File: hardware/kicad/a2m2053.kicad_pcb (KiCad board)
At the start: 2 copper layers, 100 x 110 mm, 0 parts

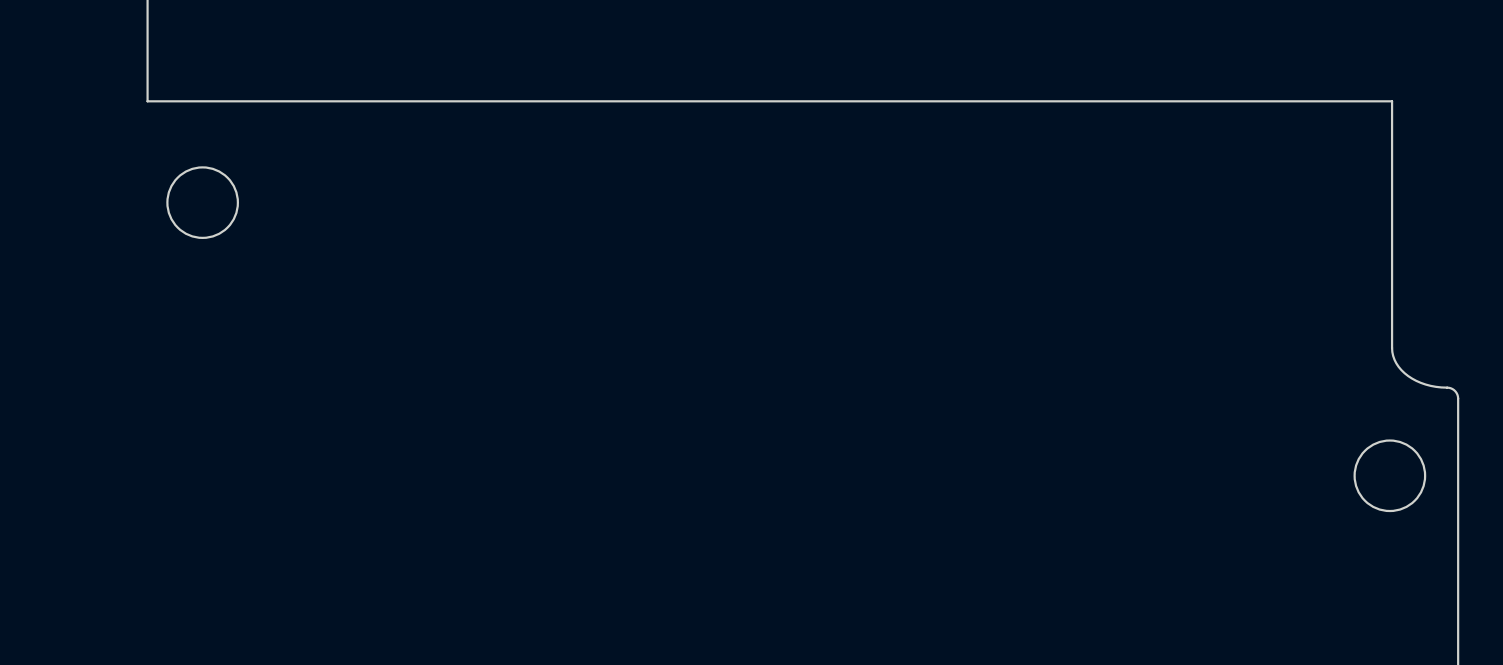
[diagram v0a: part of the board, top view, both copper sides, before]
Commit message: feat(pcb): frame-ground mounting holes H1/H2
Both M3 holes become plated footprints on net FG, placed from the
schematic. H2 uses the stock MountingHole_3.2mm_M3_Pad_Via. H1 sits
3.1 mm from the board edge, so it gets a project footprint with a
5.2 mm pad to keep 0.5 mm copper-to-edge. DRC: 0 violations; the
only unconnected item is FG between H1 and H2, not routed yet.

The outline script no longer draws hole circles; it positions H1/H2,
with a warning that footprint moves through the API crashed KiCad.

Co-Authored-By: Claude Opus 5.5 <noreply@anthropic.com>
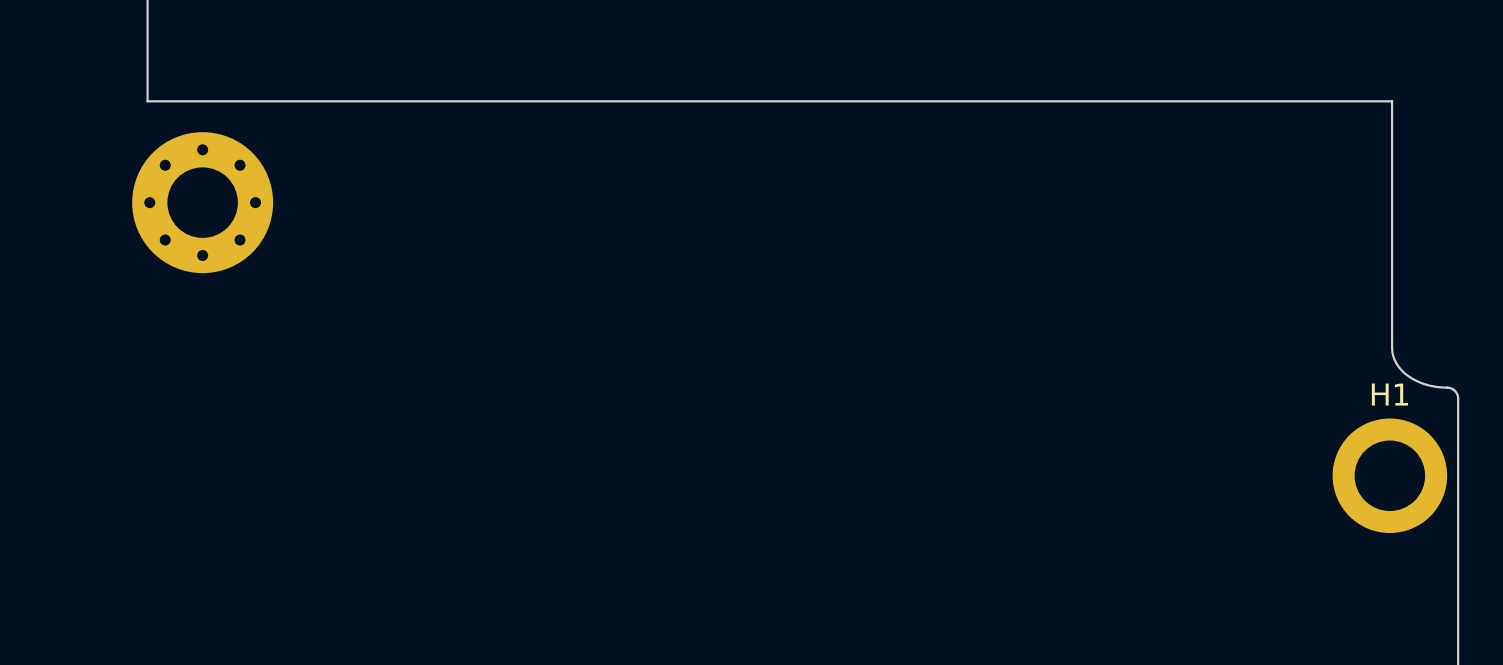
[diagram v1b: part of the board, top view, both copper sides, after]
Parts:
- added H1: M3 frame ground, a2m2053:MountingHole_3.2mm_M3_Pad_5.2mm, F.Cu at (196.9, 67.0)
- added H2: M3 frame ground, MountingHole:MountingHole_3.2mm_M3_Pad_Via, F.Cu at (143.0, 54.6)
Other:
- outline, holes or cut-outs redrawn

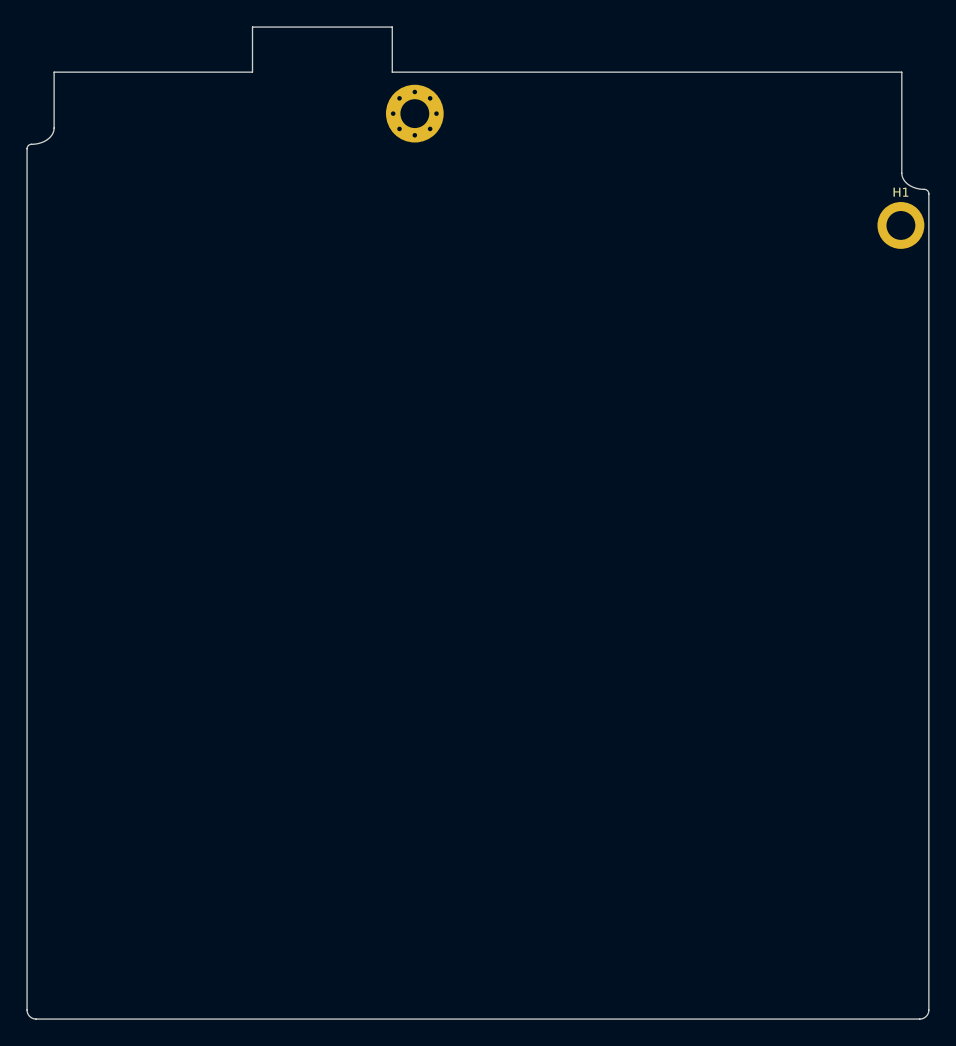
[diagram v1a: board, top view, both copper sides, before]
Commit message: feat(pcb): rear DB-19 J1 placed and fit-checked, step depths corrected
- J1: female right-angle DB-19 (daisy-chain port), 38.8 mm board-lock
  footprint on FG, face at the 94 mm top edge. Placement checked with a
  3D print holding the real connector on the IF-83 mounting points and
  in the case opening.
- Outline steps are 12 mm deep on the left and 6 mm on the right, checked
  on the IF-83. kicad_outline.py gains --outline-only.
- Photos of the fit check, EXIF stripped.

Co-Authored-By: Claude Opus 5.5 <noreply@anthropic.com>
Claude-Session: https://claude.ai/code/session_019cEGosXJSu4icn9o4uaZwB
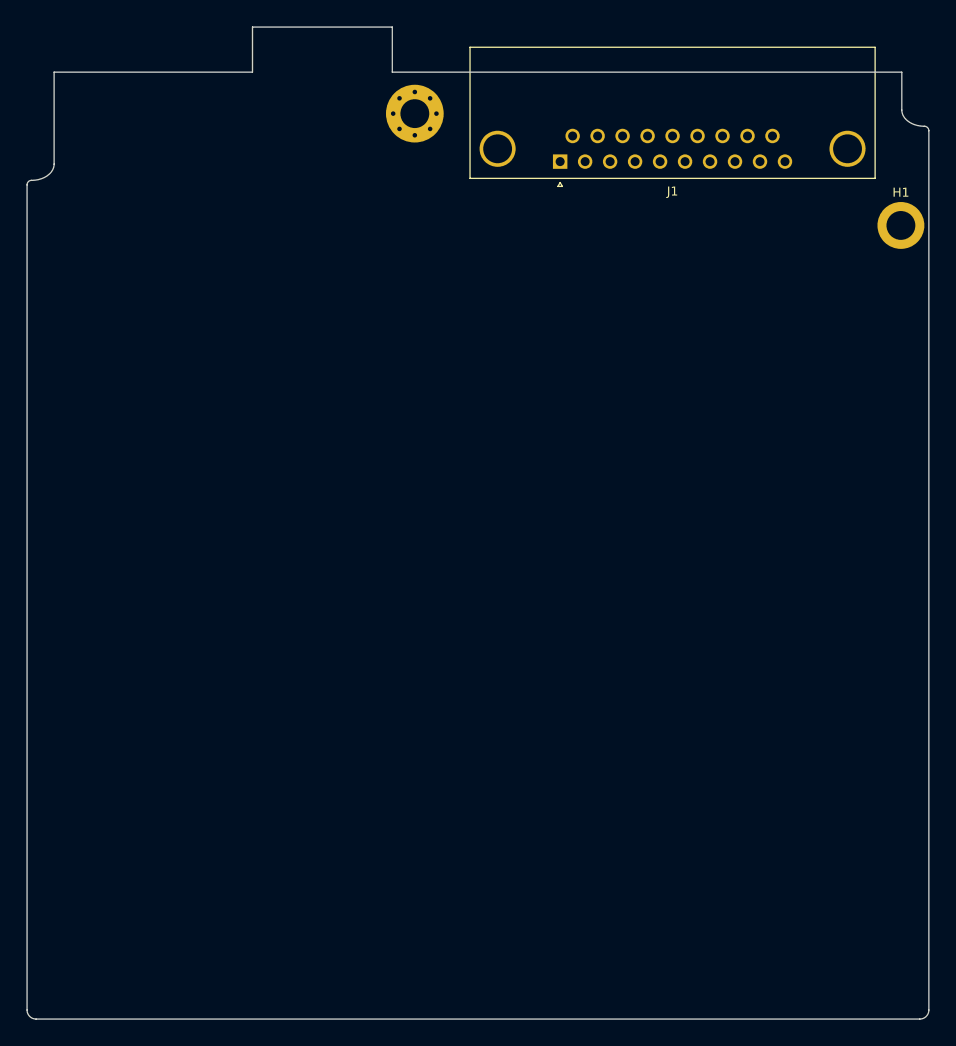
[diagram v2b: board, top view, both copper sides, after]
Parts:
- added J1: DB-19 female R/A (daisy chain), a2m2053:DSUB-19_Female_Horizontal_P2.77x2.84mm_MountingHoles38.8mm, F.Cu at (159.1, 59.9)
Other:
- outline, holes or cut-outs redrawn

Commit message: feat(pcb): schematic wired, parts placed, board autorouted
Schematic: Pico 2 (A1), five SN74LVC8T245 (U1-U5) with one 100 nF per
rail, pull-ups/pull-downs, D1 Schottky to VSYS, 4.7 uF 50 V bulk caps,
J2 (CN104) and J3 (CN102) 2x10 headers, J4 eject and J5 LED headers.

Board: all parts placed inside the IF-83 outline, Pico USB at the bottom
edge. Netclasses Power (+5V, +12V, -12V: 1.0 mm), Rail (+3V3, VSYS:
0.5 mm). GND pour on B.Cu, +5V pour on F.Cu. Tracks from Freerouting
2.1.0 (r5, 80 vias); -12V J1.5 to J3.9 routed by hand at 0.25 mm.

Routing scratch (DSN/SES runs, DRC dumps, helper scripts) lives in
hardware/kicad/scratch/, git-ignored except for its .gitkeep.

DRC: 0 unconnected. Open: EJECT via 0.42 mm from the left edge, starved
thermals on J1.4 and J3.5, silkscreen warnings, A1 library mismatch.

Co-Authored-By: Claude Opus 5.5 <noreply@anthropic.com>
Claude-Session: https://claude.ai/code/session_019cEGosXJSu4icn9o4uaZwB
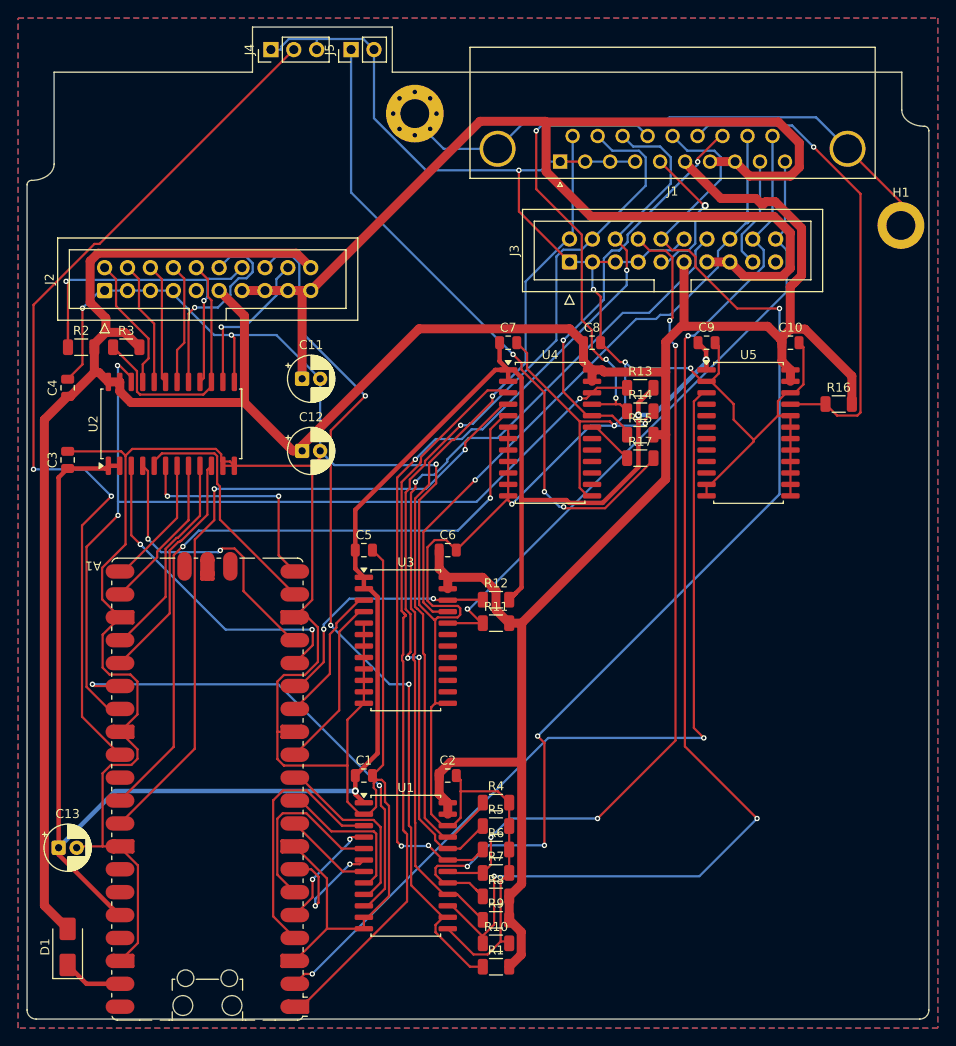
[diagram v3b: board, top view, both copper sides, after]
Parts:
- added A1: Pico 2, Module:RaspberryPi_Pico_SMD_HandSolder, F.Cu at (120.0, 129.5)
- added C1: 100nF, Capacitor_SMD:C_0805_2012Metric, F.Cu at (137.3, 128.0)
- added C10: 100nF, Capacitor_SMD:C_0805_2012Metric, F.Cu at (184.7, 80.0)
- added C11: 4.7uF 50V, Capacitor_THT:CP_Radial_D5.0mm_P2.00mm, F.Cu at (130.5, 84.0)
- added C12: 4.7uF 50V, Capacitor_THT:CP_Radial_D5.0mm_P2.00mm, F.Cu at (130.5, 92.0)
- added C13: 4.7uF 50V, Capacitor_THT:CP_Radial_D5.0mm_P2.00mm, F.Cu at (103.5, 136.0)
- added C2: 100nF, Capacitor_SMD:C_0805_2012Metric, F.Cu at (146.7, 128.0)
- added C3: 100nF, Capacitor_SMD:C_0805_2012Metric, F.Cu at (104.5, 93.0)
- added C4: 100nF, Capacitor_SMD:C_0805_2012Metric, F.Cu at (104.5, 85.0)
- added C5: 100nF, Capacitor_SMD:C_0805_2012Metric, F.Cu at (137.3, 103.0)
- added C6: 100nF, Capacitor_SMD:C_0805_2012Metric, F.Cu at (146.7, 103.0)
- added C7: 100nF, Capacitor_SMD:C_0805_2012Metric, F.Cu at (153.3, 80.0)
- added C8: 100nF, Capacitor_SMD:C_0805_2012Metric, F.Cu at (162.7, 80.0)
- added C9: 100nF, Capacitor_SMD:C_0805_2012Metric, F.Cu at (175.3, 80.0)
- added D1: STPS2L40AF, Diode_SMD:D_SMA, F.Cu at (104.5, 147.0)
- added J2: CN104 mechanism, Connector_IDC:IDC-Header_2x10_P2.54mm_Vertical, F.Cu at (108.6, 74.2)
- added J3: CN102 host (FROM HOST), Connector_IDC:IDC-Header_2x10_P2.54mm_Vertical, F.Cu at (160.2, 71.0)
- added J4: Eject button, Connector_PinHeader_2.54mm:PinHeader_1x03_P2.54mm_Vertical, F.Cu at (127.0, 47.5)
- added J5: In-use LED, Connector_PinHeader_2.54mm:PinHeader_1x02_P2.54mm_Vertical, F.Cu at (135.9, 47.5)
- added R1: 10k, Resistor_SMD:R_1206_3216Metric, F.Cu at (152.0, 149.2)
- added R10: 100k, Resistor_SMD:R_1206_3216Metric, F.Cu at (152.0, 146.6)
- added R11: 10k, Resistor_SMD:R_1206_3216Metric, F.Cu at (152.0, 111.1)
- added R12: 10k, Resistor_SMD:R_1206_3216Metric, F.Cu at (152.0, 108.5)
- added R13: 10k, Resistor_SMD:R_1206_3216Metric, F.Cu at (168.0, 85.0)
- added R14: 10k, Resistor_SMD:R_1206_3216Metric, F.Cu at (168.0, 87.6)
- added R15: 10k, Resistor_SMD:R_1206_3216Metric, F.Cu at (168.0, 90.2)
- added R16: 2k, Resistor_SMD:R_1206_3216Metric, F.Cu at (190.0, 86.8)
- added R17: 330, Resistor_SMD:R_1206_3216Metric, F.Cu at (168.0, 92.8)
- added R2: 10k, Resistor_SMD:R_1206_3216Metric, F.Cu at (106.0, 80.5)
- added R3: 10k, Resistor_SMD:R_1206_3216Metric, F.Cu at (111.0, 80.5)
- added R4: 10k, Resistor_SMD:R_1206_3216Metric, F.Cu at (152.0, 131.0)
- added R5: 10k, Resistor_SMD:R_1206_3216Metric, F.Cu at (152.0, 133.6)
- added R6: 10k, Resistor_SMD:R_1206_3216Metric, F.Cu at (152.0, 136.2)
- added R7: 10k, Resistor_SMD:R_1206_3216Metric, F.Cu at (152.0, 138.8)
- added R8: 10k, Resistor_SMD:R_1206_3216Metric, F.Cu at (152.0, 141.4)
- added R9: 10k, Resistor_SMD:R_1206_3216Metric, F.Cu at (152.0, 144.0)
- added U1: SN74LVC8T245DWR, Package_SO:SOIC-24W_7.5x15.4mm_P1.27mm, F.Cu at (142.0, 138.0)
- added U2: SN74LVC8T245DWR, Package_SO:SOIC-24W_7.5x15.4mm_P1.27mm, F.Cu at (116.0, 89.0)
- added U3: SN74LVC8T245DWR, Package_SO:SOIC-24W_7.5x15.4mm_P1.27mm, F.Cu at (142.0, 113.0)
- added U4: SN74LVC8T245DWR, Package_SO:SOIC-24W_7.5x15.4mm_P1.27mm, F.Cu at (158.0, 90.0)
- added U5: SN74LVC8T245DWR, Package_SO:SOIC-24W_7.5x15.4mm_P1.27mm, F.Cu at (180.0, 90.0)
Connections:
- J1 pad 1: (no net) -> GND
- J1 pad 10: (no net) -> /HOST_ACK
- J1 pad 11: (no net) -> /HOST_PH0
- J1 pad 12: (no net) -> /HOST_PH1
- J1 pad 13: (no net) -> /HOST_PH2
- J1 pad 14: (no net) -> /PH3_OUT
- J1 pad 15: (no net) -> /HOST_WRREQ
- J1 pad 16: (no net) -> /LASTONE
- J1 pad 17: (no net) -> /ENBL_OUT
- J1 pad 18: (no net) -> /HOST_RD
- J1 pad 19: (no net) -> /HOST_WR
- J1 pad 2: (no net) -> GND
- J1 pad 3: (no net) -> GND
- J1 pad 4: (no net) -> GND
- J1 pad 5: (no net) -> -12V
- J1 pad 6: (no net) -> +5V
- J1 pad 7: (no net) -> +12V
- J1 pad 8: (no net) -> +12V
- J1 pad 9: (no net) -> /HDSEL
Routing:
- net GND: track 0.00 -> 631.0 mm, vias 0 -> 10
- net +5V: track 0.00 -> 378.1 mm
- net +3V3: track 0.00 -> 223.4 mm, vias 0 -> 3
- net +12V: track 0.00 -> 144.2 mm
- net /HOST_WR: track 0.00 -> 129.4 mm, vias 0 -> 3
- net /HOST_WRREQ: track 0.00 -> 127.9 mm, vias 0 -> 4
- net /HOST_PH2: track 0.00 -> 110.0 mm, vias 0 -> 4
- net /U2_OE: track 0.00 -> 106.1 mm, vias 0 -> 3
- net /HOST_PH1: track 0.00 -> 105.0 mm, vias 0 -> 3
- net /EJECT: track 0.00 -> 100.5 mm, vias 0 -> 2
- net /HOST_HSTEN: track 0.00 -> 97.8 mm, vias 0 -> 1
- net /MECH_RD: track 0.00 -> 97.5 mm, vias 0 -> 3
- net /LASTONE_A: track 0.00 -> 96.2 mm, vias 0 -> 2
- net /HOST_PH0: track 0.00 -> 92.7 mm, vias 0 -> 1
- net /HOST_PH3: track 0.00 -> 91.8 mm, vias 0 -> 4
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- added copper zone on F.Cu, net +5V
- added copper zone on B.Cu, net GND

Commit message: feat(pcb): place and route the controller board
Schematic: add R18 (10k LSTRB pull-down to GND, matches the rig) and
re-order 8T245 channels on U1, U2 and U5 so the fan-outs do not cross.
HANDOFF lists the eight prototype rewires.

PCB: place all parts, route host, rear, mechanism and Pico fan-outs,
+5V and GND pours, a +12V band under the mechanism power path, stitch
the Pico GND castellations and the host pull-up pour strips. DRC with
zone refill: 0 errors; one stray via to delete in pcbnew (noted in
HANDOFF).

Co-Authored-By: Claude Fable 5.1 <noreply@anthropic.com>
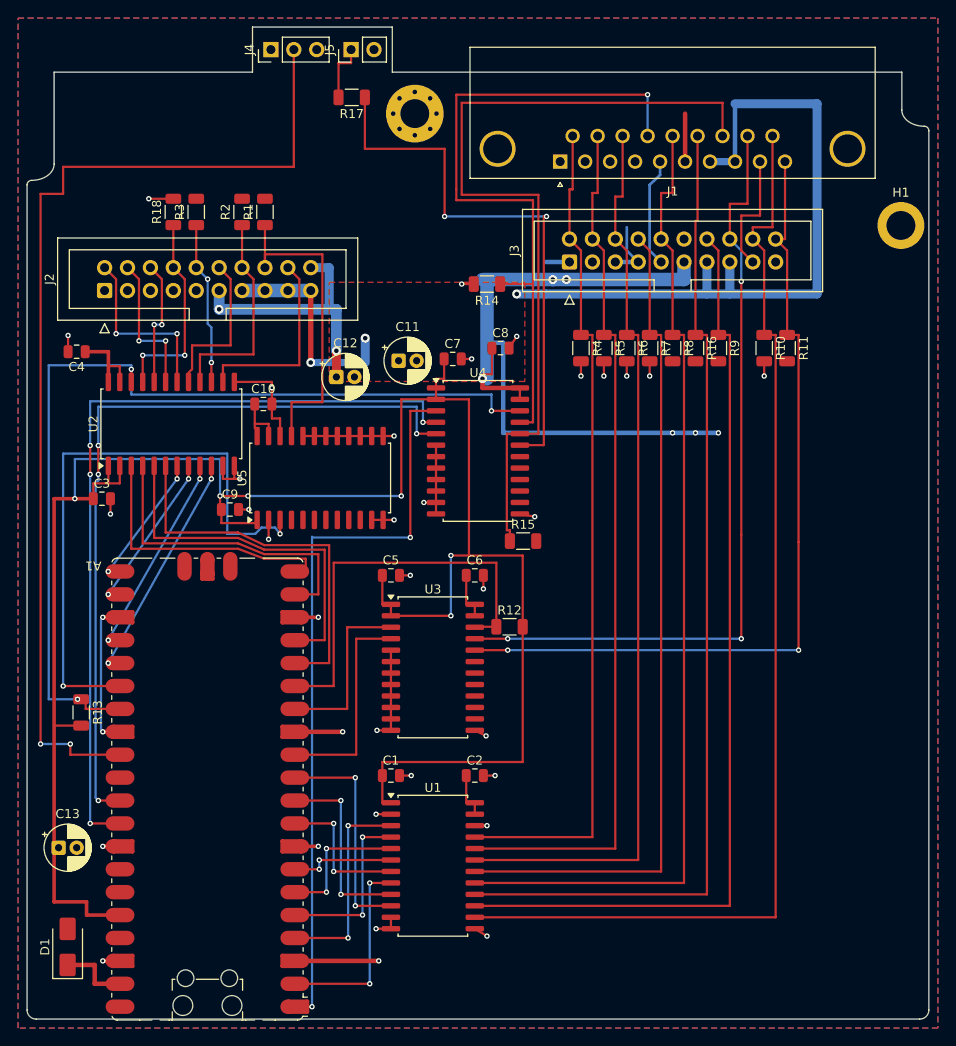
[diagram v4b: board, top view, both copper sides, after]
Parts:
- added R18: 10k, Resistor_SMD:R_1206_3216Metric, F.Cu at (116.2, 65.5)
- moved R1 87.5 mm to (126.4, 65.5), turned to 90 degrees
- moved R10 72.4 mm to (181.7, 80.6), turned to -90 degrees
- moved R13 71.7 mm to (106.0, 121.0), turned to -90 degrees
- moved R9 68.0 mm to (176.7, 80.6), turned to -90 degrees
- moved R8 63.9 mm to (171.6, 80.6), turned to -90 degrees
- moved R7 60.6 mm to (169.0, 80.6), turned to -90 degrees
- moved C10 58.8 mm to (126.2, 86.8)
- moved R6 57.5 mm to (166.5, 80.6), turned to -90 degrees
- moved C9 56.0 mm to (122.5, 98.5)
- moved R5 54.3 mm to (164.0, 80.6), turned to -90 degrees
- moved R4 51.3 mm to (161.4, 80.6), turned to -90 degrees
- moved R17 51.2 mm to (136.0, 52.8), turned to 180 degrees
- moved U5 47.8 mm to (132.5, 95.0), turned to 90 degrees
- moved R11 44.4 mm to (184.3, 80.6), turned to -90 degrees
- moved R2 23.3 mm to (123.8, 65.5), turned to 90 degrees
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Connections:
- H1 pad 1: FG -> GND
- H2 pad 1: FG -> GND
- J1 pad SH: FG -> GND
- U1 pad 10: /MECH_RD_A -> /WR_A
- U1 pad 14: /MECH_RD -> /HOST_WR
- U1 pad 15: /HOST_WR -> /HOST_HSTEN
- U1 pad 16: /HOST_HSTEN -> /LASTONE
- U1 pad 8: /HSTEN_A -> /LASTONE_A
- U1 pad 9: /WR_A -> /HSTEN_A
- U2 pad 18: /MECH_LSTRB -> /MECH_CA0
- U2 pad 19: /MECH_CA2 -> /MECH_CA1
- U2 pad 20: /MECH_CA1 -> /MECH_CA2
- U2 pad 21: /MECH_CA0 -> /MECH_LSTRB
- U2 pad 3: /CA0_A -> /LSTRB_A
- U2 pad 4: /CA1_A -> /CA2_A
- U2 pad 5: /CA2_A -> /CA1_A
- U2 pad 6: /LSTRB_A -> /CA0_A
- U5 pad 21: /LASTONE -> /MECH_RD
- U5 pad 3: /LASTONE_A -> /MECH_RD_A
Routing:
- net GND: track 631.0 -> 133.3 mm, vias 10 -> 37
- net +5V: track 378.1 -> 138.2 mm, vias 0 -> 8
- net FG: track 79.0 -> 0.00 mm
- net /LASTONE_A: track 96.2 -> 21.8 mm
- net /LED: track 73.2 -> 6.69 mm, vias 3 -> 0
- net /MECH_RD: track 97.5 -> 36.1 mm, vias 3 -> 0
- net /LASTONE: track 54.4 -> 111.3 mm, vias 1 -> 0
- net /LED_B: track 5.31 -> 61.6 mm, vias 0 -> 2
- net /ENBL_OUT: track 45.9 -> 92.5 mm, vias 2 -> 0
- net +12V: track 144.2 -> 104.1 mm, vias 0 -> 3
- net /PH3_OUT: track 53.0 -> 75.7 mm, vias 3 -> 1
- net /HOST_ACK: track 71.5 -> 92.9 mm, vias 1 -> 2
- net /MECH_ENBL: track 41.9 -> 22.8 mm, vias 2 -> 0
- net /HOST_WRREQ: track 127.9 -> 109.1 mm, vias 4 -> 0
- net /U3_OE: track 27.4 -> 45.5 mm, vias 2 -> 0
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- added copper zone on F.Cu, net +12V
